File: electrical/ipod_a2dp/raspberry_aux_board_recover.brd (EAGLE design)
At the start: 100 x 80 mm, 33 parts, among them IC1 74LS244N

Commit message: updated board
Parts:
- removed SV3: 10PIN_FEMALE, con-lsta:FE05-2
- added SV2: 10PIN_FEMALE, con-lsta:FE05-2
- added SV4: 10PIN_MALE, con-lstb:MA05-2
- C1, C2: device rcl:C025_050-035X075 -> rcl:C050-025X075
- C5: device rcl:C025_050-035X075 -> rcl:C050-050X075
- C6: device rcl:E2,5-5 -> rcl:E5-13
- R1, R2, R4, R5: device rcl:0207/10 -> rcl:0204V
- R10: device rcl:0207/10 -> rcl:0207/15
- R9: device rcl:0207/10 -> rcl:0204/7
- SV1: value 10PIN_MALE -> (none); device con-lstb:MA05-2 -> con-lstb:MA06-1
- moved IP_14 69.9 mm to (20.3, 43.2)
- moved IP_5 69.5 mm to (20.3, 47.0)
- moved IP_12 69.1 mm to (20.3, 50.8)
- moved IP_10 68.7 mm to (20.3, 54.6)
- moved IP_2 68.4 mm to (20.3, 58.4)
- moved SV1 56.2 mm to (-15.2, -7.62), turned to 0 degrees
- moved R10 51.1 mm to (10.2, 17.8), turned to 90 degrees
- moved IP_6 48.9 mm to (30.5, 45.7)
- moved IP_9 48.3 mm to (30.5, 49.5)
- moved IP_7 47.7 mm to (30.5, 53.3)
- moved IP_1 47.2 mm to (30.5, 57.1)
- moved IP_15 47.1 mm to (22.9, 61.0)
- moved IP_16 44.6 mm to (26.7, 61.0)
- moved R9 37.6 mm to (22.9, 3.81), turned to 270 degrees
- moved R5 32.0 mm to (24.1, 12.7), turned to 0 degrees
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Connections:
- net N$1 renamed PWM_AUDIO_R_OUT
- net N$4 renamed RPI_RX
- removed net N$2: R9.2, U$1.8
- removed net N$3: IC1.16, R4.1
- new net B_GND: SV1.1
- new net OR_TXD: SV1.4
- new net PWM_AUDIO_L_OUT: IC1.14, R4.1
- new net RPI_TX: R9.2, U$1.7, U$1.8
- new net Y_RXD: SV1.5
- net AUDIO_L: now also C4.-, R5.2, SV4.3; no longer C3.-, R6.2, SV1.4
- net AUDIO_L_DC: now also C1.2, C4.+, R4.2; no longer C2.2, C3.+, R1.2
- net AUDIO_L_OR: now also SV2.1; no longer SV3.2
- net AUDIO_R: now also C3.-, R6.2, SV4.1; no longer C4.-, R5.2, SV1.2
- net AUDIO_R_BR: now also SV2.3; no longer SV3.4
- net AUDIO_R_DC: now also C2.2, C3.+, R1.2; no longer C1.2, C4.+, R4.2
- net AUD_GND_B: now also SV2.2; no longer SV3.1
- net CHGR_PWR: now also SV4.6; no longer SV1.5
- net CHGR_PWR_B: now also SV2.6; no longer SV3.5
- net CONN_RECOG: now also SV4.5; no longer SV1.6
- net CONN_RECOG_Y: now also SV2.5; no longer SV3.6
- net GND: now also IC1.4, SV4.10, SV4.2; no longer IC1.6, SV1.1, SV1.9
- net IP_GND: now also SV2.4; no longer SV3.3
- net IP_RX: now also SV4.7; no longer SV1.8
- net IP_RX_P: now also SV2.7; no longer SV3.8
- net IP_TX: now also SV4.8; no longer SV1.7
- net IP_TX_GR: now also SV2.8; no longer SV3.7
- net PWM_AUD_L: now also IC1.6, U$1.33, U$1.36; no longer IC1.2, U$1.32
- net PWM_AUD_R: now also IC1.2, U$1.32; no longer IC1.4, U$1.33
- net SHIELD_RXTX_B: now also SV2.10; no longer SV3.9
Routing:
- net GND: track 0.00 -> 202.0 mm
- net RPI_TX: track 0.00 -> 77.3 mm
- net CHGR_PWR: track 0.00 -> 53.6 mm
- net VCC: track 0.00 -> 37.3 mm
- net IP_TX: track 0.00 -> 29.0 mm
- net RPI_RX: track 0.00 -> 25.0 mm
- net +5V0A: track 0.00 -> 21.4 mm
- net AUDIO_L: track 0.00 -> 15.9 mm
- net AUDIO_R: track 0.00 -> 13.8 mm
- net PWM_AUD_L: track 0.00 -> 11.3 mm
- net PWM_AUD_R: track 0.00 -> 9.77 mm
- net IP_RX: track 0.00 -> 9.72 mm
- net PWM_AUDIO_L_OUT: track 0.00 -> 8.67 mm
- net AUDIO_R_DC: track 0.00 -> 8.67 mm
- net CONN_RECOG: track 0.00 -> 7.18 mm
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- added copper zone on layer 1, net GND
- added copper zone on layer 16, net GND
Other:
- board size 100 x 80 mm -> 53 x 73.7 mm
- board text added: "jorgen@birkler.se"

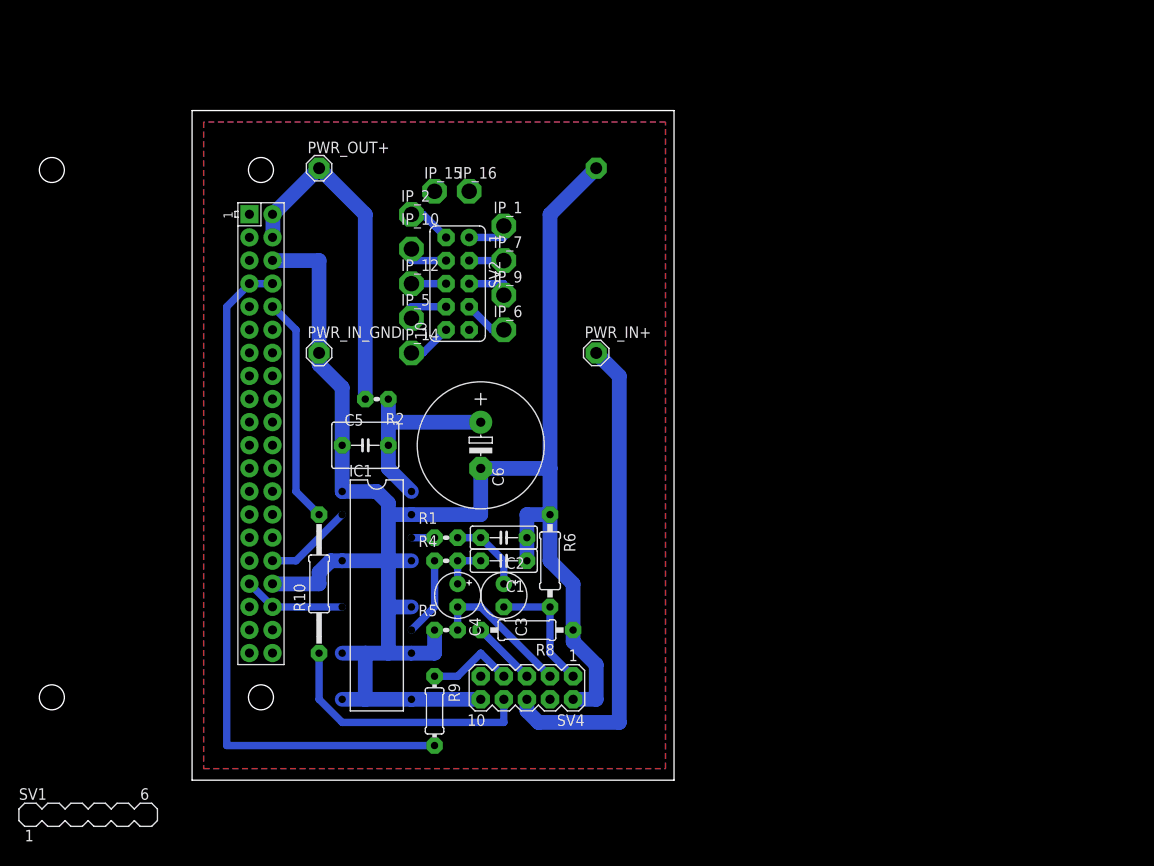
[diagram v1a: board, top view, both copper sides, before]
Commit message: update board and schematic. update daemon for ipod emul
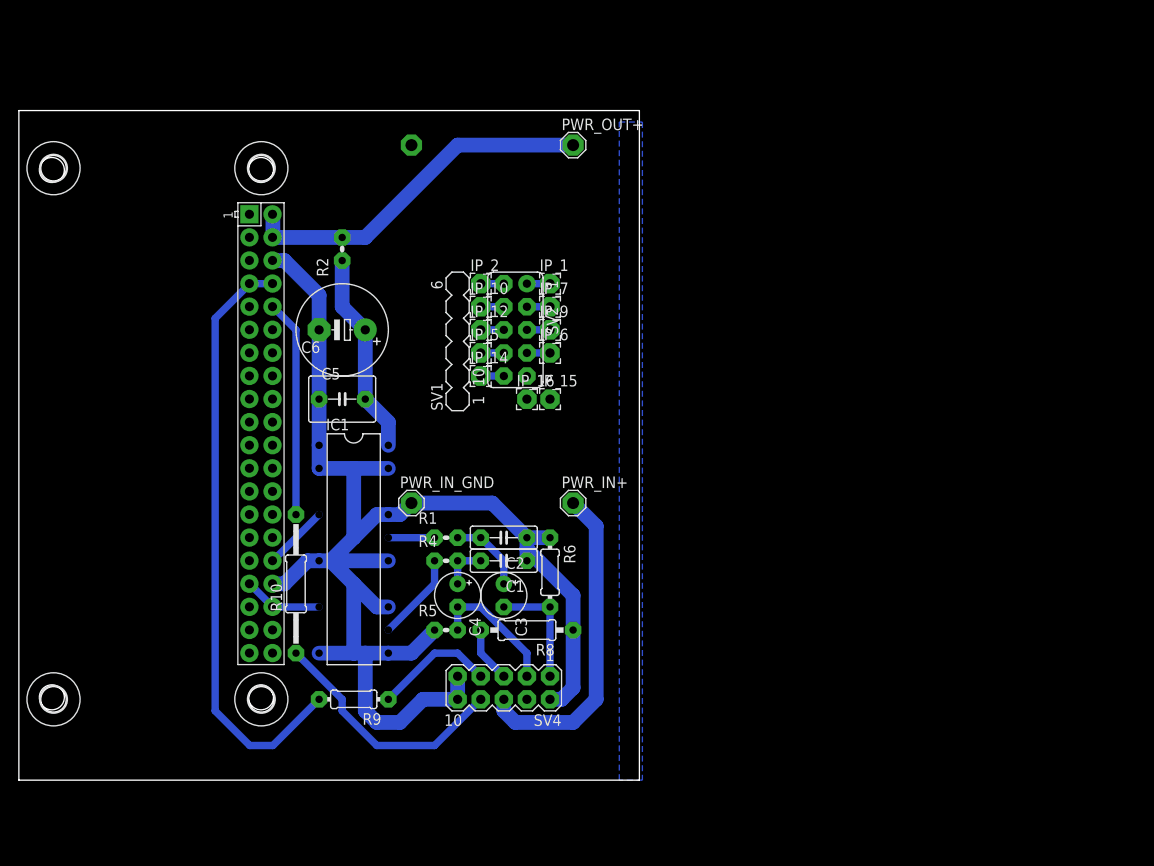
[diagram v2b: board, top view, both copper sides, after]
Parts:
- added H1, H2, H3, H4: MOUNT-HOLE2.8, holes:2,8
- C6: device rcl:E5-13 -> rcl:E5-10,5
- IP_1, IP_10, IP_12, IP_14, IP_15, IP_16, IP_2, IP_5, IP_6, IP_7, IP_9: value PTR1PAD1-17 -> X; device testpad:P1-17 -> wirepad:2,15/1,0
- R6: device rcl:0207/10 -> rcl:0204/7
- moved SV1 66.1 mm to (25.4, 44.5), turned to 90 degrees
- moved PWR_OUT+ 28.1 mm to (38.1, 66.0)
- moved IP_15 26.2 mm to (35.6, 38.1)
- moved IP_16 23.7 mm to (33.0, 38.1)
- moved PWR_OUT_GND 20.5 mm to (20.3, 66.0)
- moved C6 19.8 mm to (12.7, 45.7), turned to 180 degrees
- moved PWR_IN_GND 19.4 mm to (20.3, 26.7)
- moved R2 16.9 mm to (12.7, 54.6), turned to 90 degrees
- moved PWR_IN+ 16.7 mm to (38.1, 26.7)
- moved IP_2 10.8 mm to (27.9, 50.8)
- moved IP_10 9.92 mm to (27.9, 48.3)
- moved IP_12 9.16 mm to (27.9, 45.7)
- moved R9 8.98 mm to (14.0, 5.08), turned to 180 degrees
- moved IP_5 8.52 mm to (27.9, 43.2)
- moved IP_1 8.13 mm to (35.6, 50.8)
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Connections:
- removed net PWM_AUDIO_L_OUT: IC1.14, R4.1
- removed net PWM_AUDIO_R_OUT: IC1.18, R1.1
- new net N$1: IC1.12, R4.1
- new net N$2: IC1.16, R1.1
- net ACC_DETECT_W: now also IP_15.1; no longer IP_15.TP
- net ACC_ID_R: now also IP_16.1; no longer IP_16.TP
- net AUDIO_L_OR: now also IP_1.1; no longer IP_1.TP
- net AUDIO_R_BR: now also IP_7.1; no longer IP_7.TP
- net AUD_GND_B: now also IP_2.1; no longer IP_2.TP
- net CHGR_PWR_B: now also IP_12.1; no longer IP_12.TP
- net CONN_RECOG_Y: now also IP_9.1; no longer IP_9.TP
- net GND: now also IC1.2, IC1.6, SV4.9; no longer IC1.4, IC1.8, PWR_OUT_GND.MP
- net IP_GND: now also IP_10.1; no longer IP_10.TP
- net IP_RX_P: now also IP_6.1; no longer IP_6.TP
- net IP_TX_GR: now also IP_5.1; no longer IP_5.TP
- net PWM_AUD_L: now also IC1.8; no longer IC1.6
- net PWM_AUD_R: now also IC1.4; no longer IC1.2
- net SHIELD_RXTX_B: now also IP_14.1; no longer IP_14.TP
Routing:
- net GND: track 202.0 -> 156.5 mm
- net CHGR_PWR: track 53.6 -> 35.7 mm
- net RPI_TX: track 77.3 -> 66.3 mm
- net N$1: track 0.00 -> 9.72 mm
- net PWM_AUDIO_L_OUT: track 8.67 -> 0.00 mm
- net N$2: track 0.00 -> 5.08 mm
- net IP_RX: track 9.72 -> 13.3 mm
- net VCC: track 37.3 -> 39.9 mm
- net PWM_AUD_L: track 11.3 -> 8.76 mm
- net PWM_AUDIO_R_OUT: track 2.54 -> 0.00 mm
- net PWM_AUD_R: track 9.77 -> 7.23 mm
- net IP_TX_GR: track 5.08 -> 2.54 mm
- net IP_GND: track 5.08 -> 2.54 mm
- net CONN_RECOG_Y: track 5.08 -> 2.54 mm
- net AUDIO_L_OR: track 5.08 -> 2.54 mm
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- removed copper zone on layer 1, net GND
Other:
- board size 53 x 73.7 mm -> 68.2 x 73.7 mm

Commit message: updated schematic and board. sent to production
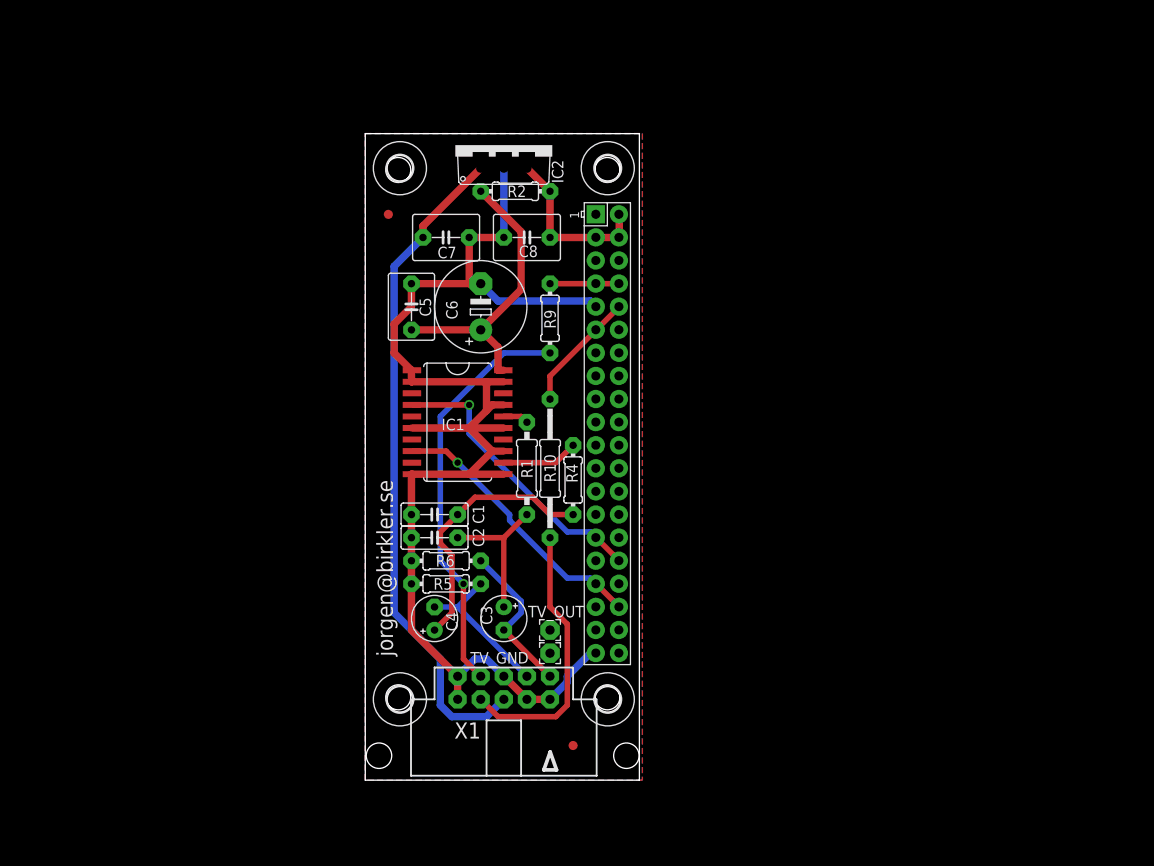
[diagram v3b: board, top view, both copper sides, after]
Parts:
- removed IP_1, IP_10, IP_12, IP_14, IP_15, IP_16, IP_2, IP_5, IP_6, IP_7, IP_9: X, wirepad:2,15/1,0
- removed PWR_IN+, PWR_IN_GND, PWR_OUT+, PWR_OUT_GND: SE13, solpad:SE13
- removed R8: 0R, rcl:0207/10
- removed SV1: (no value), con-lstb:MA06-1
- removed SV2: 10PIN_FEMALE, con-lsta:FE05-2
- removed SV4: 10PIN_MALE, con-lstb:MA05-2
- added C7, C8: 220n, rcl:C050-050X075
- added IC2: 788TV, linear:TO220V
- added TV_GND, TV_OUT: (no value), wirepad:2,15/1,0
- added U$2, U$3: FIDUCIAL, adafruit:FIDUCIAL_1MM
- added X1: 057-010-0, con-panduit:057-010-0
- IC1: value 74LS244N -> 74LS244DW; device 74xx-us:DIL20 -> 74xx-us:SO20W
- R1: device rcl:0204V -> rcl:0207/10
- R2, R4, R5: device rcl:0204V -> rcl:0204/7
- moved R9 47.1 mm to (35.6, 47.0), turned to 90 degrees
- moved H1 38.1 mm to (19.1, 5.08)
- moved H4 38.1 mm to (19.1, 63.5)
- moved U$1 38.1 mm to (15.4, 66.8)
- moved H2 38.1 mm to (41.9, 5.08)
- moved H3 38.1 mm to (41.9, 63.5)
- moved R10 30.7 mm to (35.6, 30.5)
- moved R2 20.1 mm to (31.8, 61.0), turned to 0 degrees
- moved IC1 18.1 mm to (25.4, 35.6)
- moved R4 16.6 mm to (38.1, 29.2), turned to 270 degrees
- moved C6 15.5 mm to (27.9, 48.3), turned to 90 degrees
- moved C5 12.7 mm to (20.3, 48.3), turned to 270 degrees
- moved R1 11.7 mm to (33.0, 30.5), turned to 270 degrees
- moved R6 11.5 mm to (24.1, 20.3), turned to 0 degrees
- moved C1 9.16 mm to (22.9, 25.4), turned to 0 degrees
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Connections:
- removed net ACC_DETECT_W: IP_15.1
- removed net ACC_ID_R: IP_16.1
- removed net AUDIO_L_OR: IP_1.1, SV2.1
- removed net AUDIO_R_BR: IP_7.1, SV2.3
- removed net AUD_GND_B: IP_2.1, SV2.2
- removed net B_GND: SV1.1
- removed net CHGR_PWR_B: IP_12.1, SV2.6
- removed net CONN_RECOG: R8.2, SV4.5
- removed net CONN_RECOG_Y: IP_9.1, SV2.5
- removed net IP_GND: IP_10.1, SV2.4
- removed net IP_RX_P: IP_6.1, SV2.7
- removed net IP_TX_GR: IP_5.1, SV2.8
- removed net OR_TXD: SV1.4
- removed net SHIELD_RXTX_B: IP_14.1, SV2.10
- removed net Y_RXD: SV1.5
- new net TV_OUT: TV_OUT.1
- net AUDIO_L: now also X1.3; no longer SV4.3
- net AUDIO_R: now also X1.1; no longer SV4.1
- net CHGR_PWR: now also C7.2, IC2.1, X1.6; no longer PWR_IN+.MP, SV4.6
- net GND: now also C7.1, C8.1, IC2.2, U$1.39, U$1.9, X1.10, X1.2, X1.4, X1.5, X1.9; no longer PWR_IN_GND.MP, R8.1, SV4.10, SV4.2, SV4.9, U$1.34, U$1.6
- net IP_RX: now also X1.7; no longer SV4.7
- net IP_TX: now also X1.8; no longer SV4.8
- net PWM_AUD_R: now also U$1.29
- net RPI_RX: now also U$1.11
- net VCC: now also C8.2, IC2.3, U$1.3; no longer PWR_OUT+.MP
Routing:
- net RPI_TX: track 66.3 -> 7.58 mm
- net CHGR_PWR: track 35.7 -> 73.4 mm
- net IP_RX: track 13.3 -> 45.4 mm, vias 0 -> 1
- net PWM_AUD_R: track 7.23 -> 31.7 mm, vias 0 -> 1
- net AUDIO_L_DC: track 5.08 -> 29.1 mm
- net PWM_AUD_L: track 8.76 -> 30.3 mm, vias 0 -> 1
- net VCC: track 39.9 -> 18.8 mm
- net GND: track 156.5 -> 144.1 mm
- net RPI_RX: track 24.0 -> 13.7 mm
- net +5V0A: track 22.4 -> 32.4 mm
- net AUDIO_R_DC: track 8.67 -> 16.3 mm
- net CONN_RECOG: track 6.13 -> 0.00 mm
- net AUDIO_R: track 12.7 -> 17.4 mm
- net IP_TX: track 27.4 -> 30.0 mm
- net SHIELD_RXTX_B: track 2.54 -> 0.00 mm
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- added copper zone on layer 1, net GND
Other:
- board size 68.2 x 73.7 mm -> 30.1 x 71.1 mm

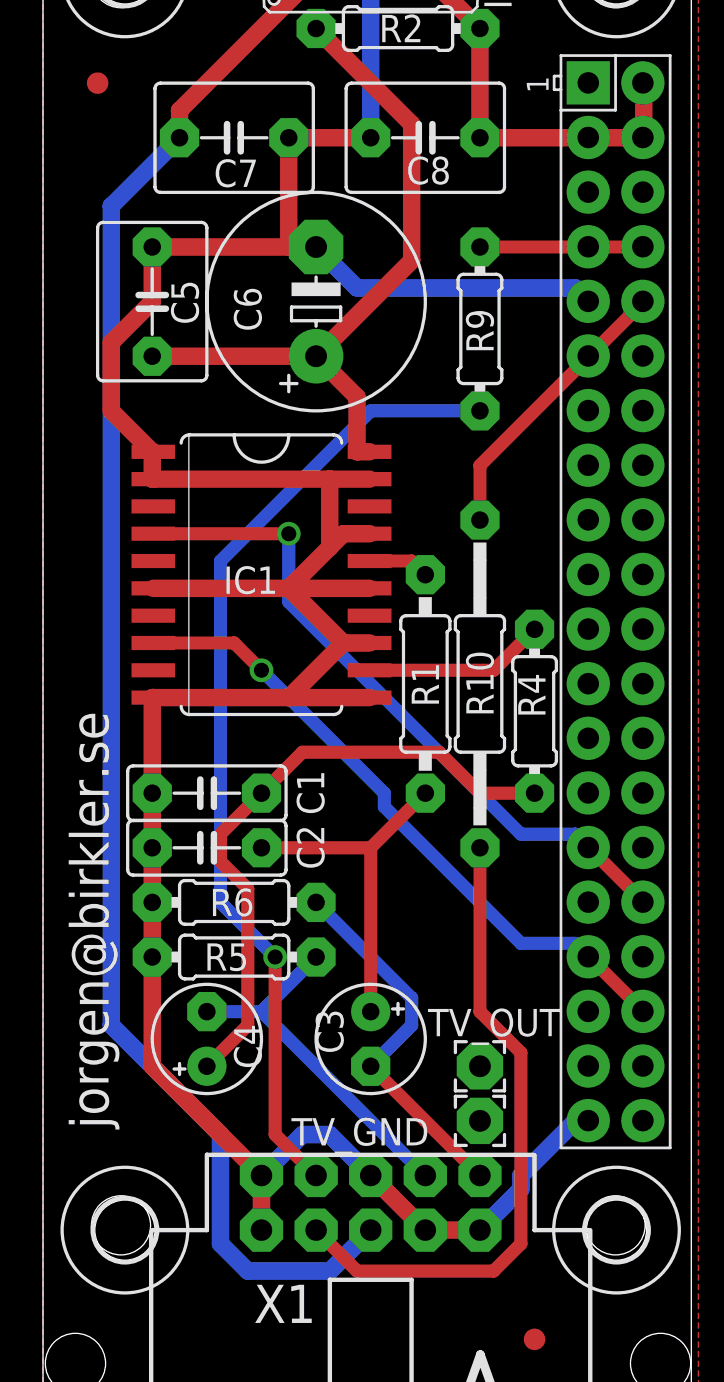
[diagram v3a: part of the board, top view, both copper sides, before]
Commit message: New CAM production with soldermask plus fixes to silkmask
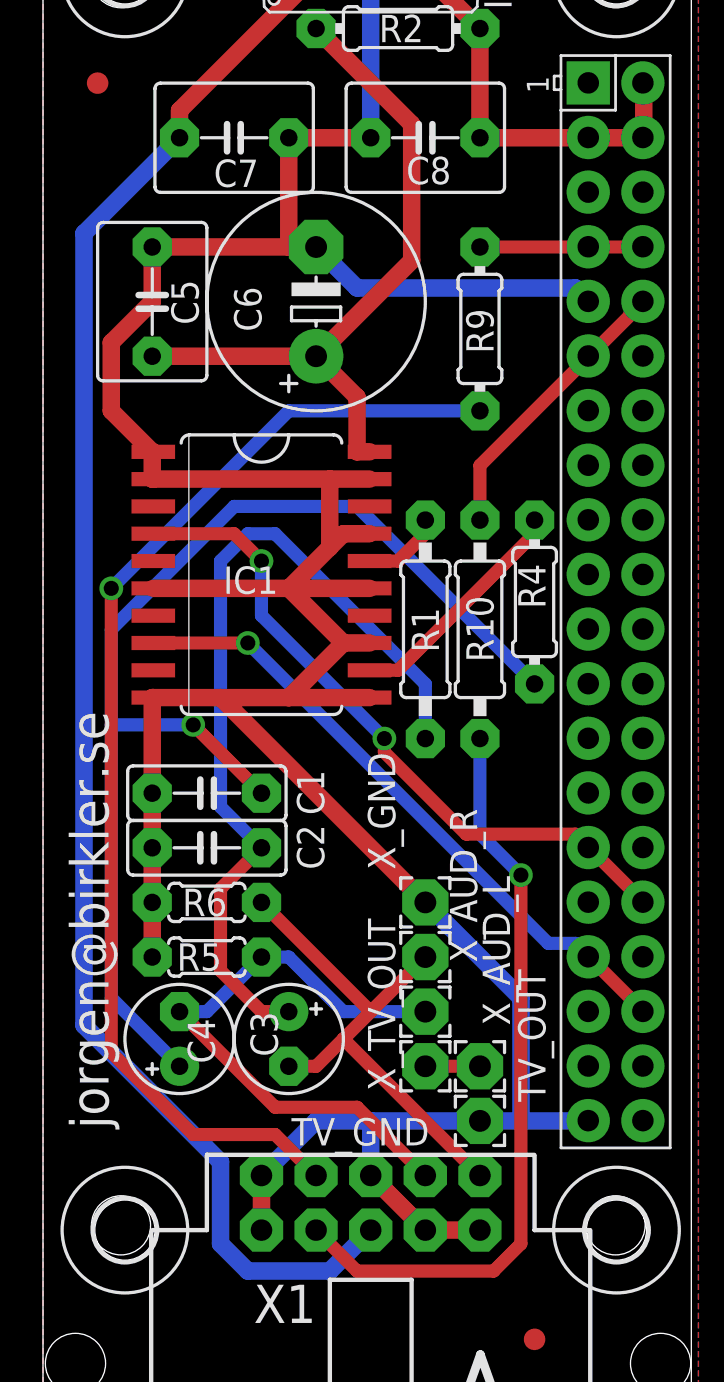
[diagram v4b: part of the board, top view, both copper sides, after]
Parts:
- added X_AUD_L, X_AUD_R, X_GND, X_TV_OUT: x, wirepad:2,15/1,0
- R10: device rcl:0207/15 -> rcl:0207/10
- R5, R6: device rcl:0204/7 -> rcl:0204/5
- TV_GND, TV_OUT: value (none) -> x
- moved R4 5.08 mm to (38.1, 34.3)
- moved C3 3.81 mm to (26.7, 14.0)
- moved R1 2.54 mm to (33.0, 33.0)
- moved R10 2.54 mm to (35.6, 33.0)
- moved C4 1.27 mm to (21.6, 14.0)
- moved R5 1.27 mm to (22.9, 17.8)
- moved R6 1.27 mm to (22.9, 20.3)
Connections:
- net AUDIO_L: now also X_AUD_L.1
- net AUDIO_R: now also X_AUD_R.1
- net GND: now also TV_GND.1, X_GND.1
- net TV_OUT: now also X_TV_OUT.1
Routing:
- net AUDIO_L_DC: track 29.1 -> 55.4 mm, vias 0 -> 1
- net AUDIO_R_DC: track 16.3 -> 40.1 mm
- net GND: track 144.1 -> 161.9 mm
- net AUDIO_L: track 16.9 -> 28.1 mm
- net IP_RX: track 45.4 -> 54.0 mm
- net AUDIO_R: track 17.4 -> 24.6 mm
- net IP_TX: track 30.0 -> 35.1 mm, vias 0 -> 1
- net TV_OUT: track 0.00 -> 2.54 mm
- net N$1: track 8.46 -> 10.9 mm
- net CHGR_PWR: track 73.4 -> 74.5 mm
- net N$2: track 2.85 -> 3.75 mm
- net PWM_AUD_R: vias 1 -> 2
